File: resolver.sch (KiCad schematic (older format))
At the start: 17 parts, among them U4 TDA2822D

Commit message: fixed schematics error
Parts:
- C20, C21, C22, C23, C24, C25, C26, C27, C28, C29: symbol prius_gen2-rescue:C-Device -> prius_gen2-rescue:C-Device-prius_gen2-rescue
- R27, R28, R29, R30, R31, R32: symbol prius_gen2-rescue:R-Device -> prius_gen2-rescue:R-Device-prius_gen2-rescue
- U4: symbol prius_gen2-rescue:TDA2822D-TDA2822D -> prius_gen2-rescue:TDA2822D-TDA2822D-prius_gen2-rescue
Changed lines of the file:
@@
 TIM3_ETR
 $Comp
-L prius_gen2-rescue:R-Device R27
+L prius_gen2-rescue:R-Device-prius_gen2-rescue R27
 U 1 1 60EAC28E
 P 4275 3050
@@
 $EndComp
 $Comp
-L prius_gen2-rescue:R-Device R28
+L prius_gen2-rescue:R-Device-prius_gen2-rescue R28
 U 1 1 60EAC478
 P 4750 3050
@@
 $EndComp
 $Comp
-L prius_gen2-rescue:R-Device R29
+L prius_gen2-rescue:R-Device-prius_gen2-rescue R29
 U 1 1 60EAC5BA
 P 5225 3050
@@
 $EndComp
 $Comp
-L prius_gen2-rescue:R-Device R30
+L prius_gen2-rescue:R-Device-prius_gen2-rescue R30
 U 1 1 60EAC728
 P 5975 3275
@@
 	5075 3050 4975 3050
 $Comp
-L prius_gen2-rescue:C-Device C22
+L prius_gen2-rescue:C-Device-prius_gen2-rescue C22
 U 1 1 60EACE0E
 P 4500 3300
@@
 $EndComp
 $Comp
-L prius_gen2-rescue:C-Device C23
+L prius_gen2-rescue:C-Device-prius_gen2-rescue C23
 U 1 1 60EAD11D
 P 4975 3300
@@
 $EndComp
 $Comp
-L prius_gen2-rescue:C-Device C24
+L prius_gen2-rescue:C-Device-prius_gen2-rescue C24
 U 1 1 60EAD325
 P 5450 3300
@@
 $EndComp
 $Comp
-L prius_gen2-rescue:C-Device C25
+L prius_gen2-rescue:C-Device-prius_gen2-rescue C25
 U 1 1 60EADA96
 P 5650 3050
@@
 	5975 3050 5975 3125
 $Comp
-L prius_gen2-rescue:GND-power #PWR0140
+L prius_gen2-rescue:GND-power-prius_gen2-rescue #PWR0140
 U 1 1 60EAFA6D
 P 7025 3550
@@
 Resolver Excitation
 $Comp
-L prius_gen2-rescue:+5V-power #PWR0141
+L prius_gen2-rescue:+5V-power-prius_gen2-rescue #PWR0141
 U 1 1 60EBE0BA
 P 4050 3900
@@
 $EndComp
 $Comp
-L prius_gen2-rescue:C-Device C20
+L prius_gen2-rescue:C-Device-prius_gen2-rescue C20
 U 1 1 60EBE262
 P 3850 4150
@@
 $EndComp
 $Comp
-L prius_gen2-rescue:C-Device C21
+L prius_gen2-rescue:C-Device-prius_gen2-rescue C21
 U 1 1 60EBE45E
 P 4225 4150
@@
 $EndComp
 $Comp
-L prius_gen2-rescue:GND-power #PWR0142
+L prius_gen2-rescue:GND-power-prius_gen2-rescue #PWR0142
 U 1 1 60EBEB3E
 P 4050 4400
@@
 Connection ~ 4050 3950
 $Comp
-L prius_gen2-rescue:TDA2822D-TDA2822D U4
+L prius_gen2-rescue:TDA2822D-TDA2822D-prius_gen2-rescue U4
 U 1 1 61606D5B
 P 6925 2950
@@
 $EndComp
 $Comp
-L prius_gen2-rescue:TDA2822D-TDA2822D U4
+L prius_gen2-rescue:TDA2822D-TDA2822D-prius_gen2-rescue U4
 U 2 1 616074FB
 P 6925 4250
@@
 	7800 2950 7575 2950
 $Comp
-L prius_gen2-rescue:R-Device R31
+L prius_gen2-rescue:R-Device-prius_gen2-rescue R31
 U 1 1 6160E8C8
 P 7575 3175
@@
 $EndComp
 $Comp
-L prius_gen2-rescue:C-Device C28
+L prius_gen2-rescue:C-Device-prius_gen2-rescue C28
 U 1 1 6160EF84
 P 7575 3575
@@
 $EndComp
 $Comp
-L prius_gen2-rescue:GND-power #PWR0143
+L prius_gen2-rescue:GND-power-prius_gen2-rescue #PWR0143
 U 1 1 61611699
 P 7575 3825
@@
 	7575 3425 7575 3325
 $Comp
-L prius_gen2-rescue:+5V-power #PWR0144
+L prius_gen2-rescue:+5V-power-prius_gen2-rescue #PWR0144
 U 1 1 616132D9
 P 7025 2550
@@
 	7025 2550 7025 2650
 $Comp
-L prius_gen2-rescue:R-Device R32
+L prius_gen2-rescue:R-Device-prius_gen2-rescue R32
 U 1 1 61615A70
 P 7575 4475
@@
 $EndComp
 $Comp
-L prius_gen2-rescue:C-Device C29
+L prius_gen2-rescue:C-Device-prius_gen2-rescue C29
 U 1 1 61615B04
 P 7575 4875
@@
 $EndComp
 $Comp
-L prius_gen2-rescue:GND-power #PWR0145
+L prius_gen2-rescue:GND-power-prius_gen2-rescue #PWR0145
 U 1 1 61615B0E
 P 7575 5125
@@
 Connection ~ 5975 3050
 $Comp
-L prius_gen2-rescue:C-Device C27
+L prius_gen2-rescue:C-Device-prius_gen2-rescue C27
 U 1 1 6161DBD5
 P 6550 3825
@@
 $EndComp
 $Comp
-L prius_gen2-rescue:C-Device C26
+L prius_gen2-rescue:C-Device-prius_gen2-rescue C26
 U 1 1 6161E12E
 P 6325 3825

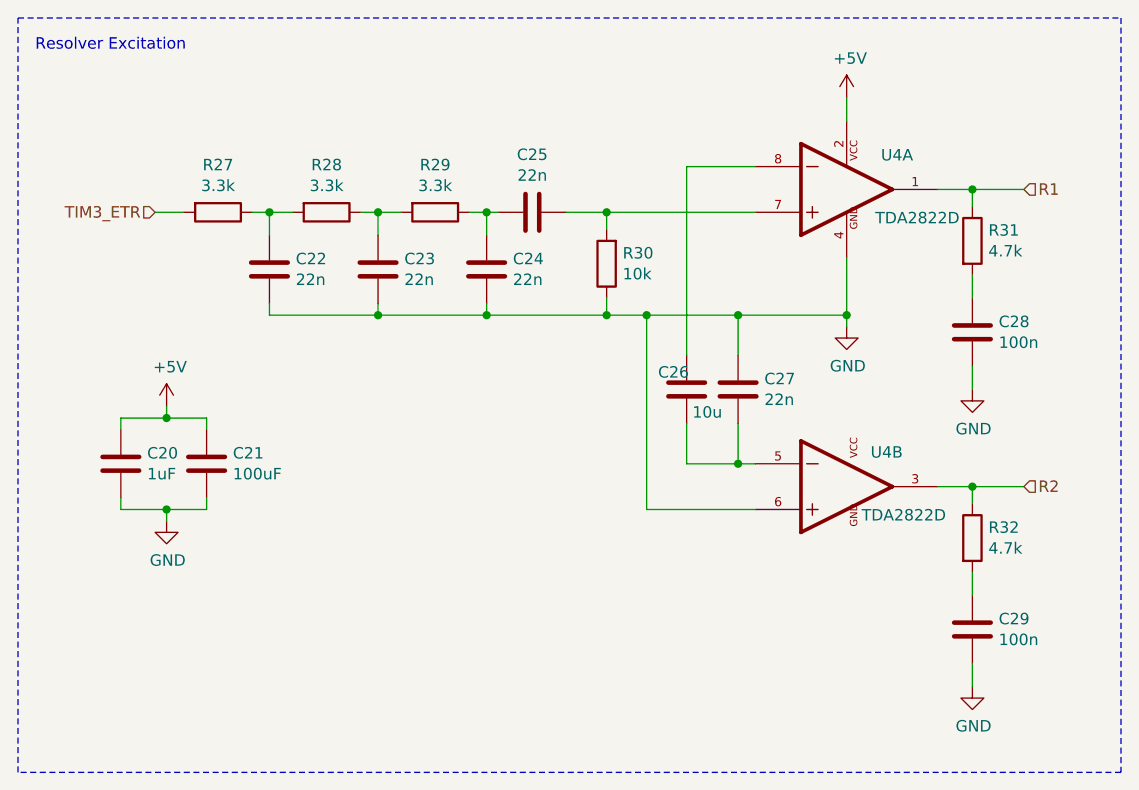
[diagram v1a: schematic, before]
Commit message: updated vals for 3stage RC filter
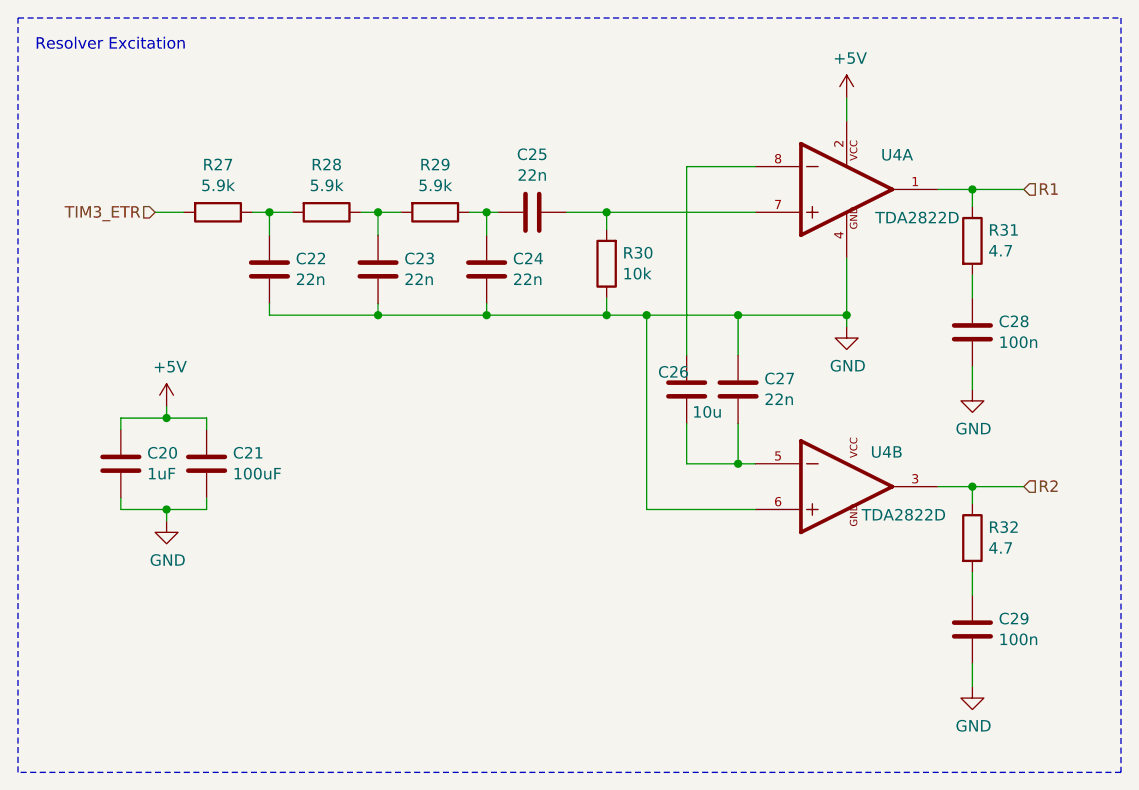
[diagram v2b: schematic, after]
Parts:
- R27, R28, R29: value 3.3k -> 5.9k
- R31, R32: value 4.7k -> 4.7
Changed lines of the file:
@@
 TIM3_ETR
-$Comp
-L prius_gen2-rescue:R-Device-prius_gen2-rescue R27
-U 1 1 60EAC28E
-P 4275 3050
-F 0 "R27" V 4068 3050 50  0000 C CNN
-F 1 "3.3k" V 4159 3050 50  0000 C CNN
-F 2 "Resistor_SMD:R_0603_1608Metric" V 4205 3050 50  0001 C CNN
-F 3 "~" H 4275 3050 50  0001 C CNN
-	1    4275 3050
-	0    1    1    0
-$EndComp
-$Comp
-L prius_gen2-rescue:R-Device-prius_gen2-rescue R28
-U 1 1 60EAC478
-P 4750 3050
-F 0 "R28" V 4543 3050 50  0000 C CNN
-F 1 "3.3k" V 4634 3050 50  0000 C CNN
-F 2 "Resistor_SMD:R_0603_1608Metric" V 4680 3050 50  0001 C CNN
-F 3 "~" H 4750 3050 50  0001 C CNN
-	1    4750 3050
-	0    1    1    0
-$EndComp
-$Comp
-L prius_gen2-rescue:R-Device-prius_gen2-rescue R29
-U 1 1 60EAC5BA
-P 5225 3050
-F 0 "R29" V 5018 3050 50  0000 C CNN
-F 1 "3.3k" V 5109 3050 50  0000 C CNN
-F 2 "Resistor_SMD:R_0603_1608Metric" V 5155 3050 50  0001 C CNN
-F 3 "~" H 5225 3050 50  0001 C CNN
-	1    5225 3050
-	0    1    1    0
-$EndComp
 $Comp
 L prius_gen2-rescue:R-Device-prius_gen2-rescue R30
@@
 P 7575 3175
 F 0 "R31" H 7645 3221 50  0000 L CNN
-F 1 "4.7k" H 7645 3130 50  0000 L CNN
+F 1 "4.7" H 7645 3130 50  0000 L CNN
 F 2 "Resistor_SMD:R_0603_1608Metric" V 7505 3175 50  0001 C CNN
 F 3 "~" H 7575 3175 50  0001 C CNN
@@
 P 7575 4475
 F 0 "R32" H 7645 4521 50  0000 L CNN
-F 1 "4.7k" H 7645 4430 50  0000 L CNN
+F 1 "4.7" H 7645 4430 50  0000 L CNN
 F 2 "Resistor_SMD:R_0603_1608Metric" V 7505 4475 50  0001 C CNN
 F 3 "~" H 7575 4475 50  0001 C CNN
@@
 Wire Wire Line
 	4050 4350 4225 4350
+$Comp
+L prius_gen2-rescue:R-Device-prius_gen2-rescue R29
+U 1 1 60EAC5BA
+P 5225 3050
+F 0 "R29" V 5018 3050 50  0000 C CNN
+F 1 "5.9k" V 5109 3050 50  0000 C CNN
+F 2 "Resistor_SMD:R_0603_1608Metric" V 5155 3050 50  0001 C CNN
+F 3 "~" H 5225 3050 50  0001 C CNN
+	1    5225 3050
+	0    1    1    0
+$EndComp
+$Comp
+L prius_gen2-rescue:R-Device-prius_gen2-rescue R28
+U 1 1 60EAC478
+P 4750 3050
+F 0 "R28" V 4543 3050 50  0000 C CNN
+F 1 "5.9k" V 4634 3050 50  0000 C CNN
+F 2 "Resistor_SMD:R_0603_1608Metric" V 4680 3050 50  0001 C CNN
+F 3 "~" H 4750 3050 50  0001 C CNN
+	1    4750 3050
+	0    1    1    0
+$EndComp
+$Comp
+L prius_gen2-rescue:R-Device-prius_gen2-rescue R27
+U 1 1 60EAC28E
+P 4275 3050
+F 0 "R27" V 4068 3050 50  0000 C CNN
+F 1 "5.9k" V 4159 3050 50  0000 C CNN
+F 2 "Resistor_SMD:R_0603_1608Metric" V 4205 3050 50  0001 C CNN
+F 3 "~" H 4275 3050 50  0001 C CNN
+	1    4275 3050
+	0    1    1    0
+$EndComp
 $EndSCHEMATC

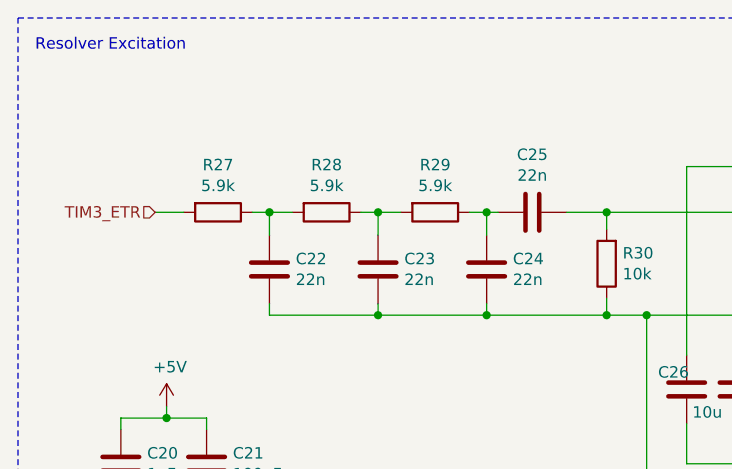
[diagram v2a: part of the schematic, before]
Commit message: more updates to RC filter; fixed pinout silk
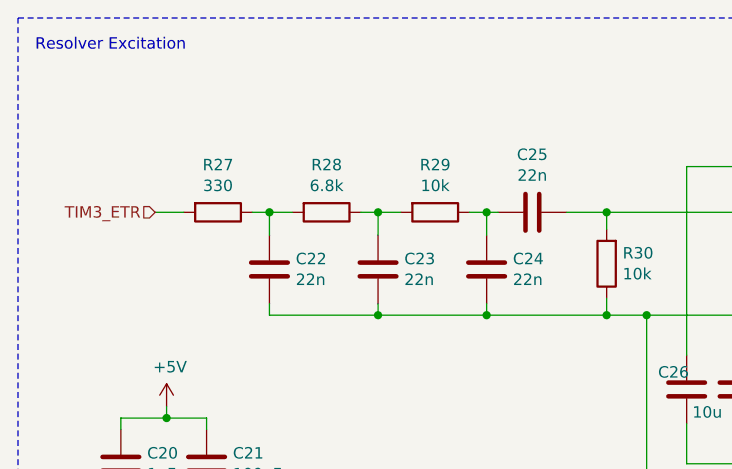
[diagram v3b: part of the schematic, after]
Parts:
- R27: value 5.9k -> 330
- R28: value 5.9k -> 6.8k
- R29: value 5.9k -> 10k
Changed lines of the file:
@@
 P 5225 3050
 F 0 "R29" V 5018 3050 50  0000 C CNN
-F 1 "5.9k" V 5109 3050 50  0000 C CNN
+F 1 "10k" V 5109 3050 50  0000 C CNN
 F 2 "Resistor_SMD:R_0603_1608Metric" V 5155 3050 50  0001 C CNN
 F 3 "~" H 5225 3050 50  0001 C CNN
@@
 P 4750 3050
 F 0 "R28" V 4543 3050 50  0000 C CNN
-F 1 "5.9k" V 4634 3050 50  0000 C CNN
+F 1 "6.8k" V 4634 3050 50  0000 C CNN
 F 2 "Resistor_SMD:R_0603_1608Metric" V 4680 3050 50  0001 C CNN
 F 3 "~" H 4750 3050 50  0001 C CNN
@@
 P 4275 3050
 F 0 "R27" V 4068 3050 50  0000 C CNN
-F 1 "5.9k" V 4159 3050 50  0000 C CNN
+F 1 "330" V 4159 3050 50  0000 C CNN
 F 2 "Resistor_SMD:R_0603_1608Metric" V 4205 3050 50  0001 C CNN
 F 3 "~" H 4275 3050 50  0001 C CNN
